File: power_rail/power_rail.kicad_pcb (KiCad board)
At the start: 2 copper layers, 100 x 50 mm, 18 parts, among them J1 Conn_01x06, J2 Conn_02x08_Row_Letter_Last, J3 Conn_02x08_Row_Letter_Last, J4 Conn_02x08_Row_Letter_Last, J5 Conn_02x08_Row_Letter_Last, J6 Conn_02x08_Row_Letter_Last, J7 Conn_02x08_Row_Letter_Last, J8 Conn_01x06

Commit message: VCA v. 2.0
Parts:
- added J11: Conn_01x01_Pin, power_rail_elements:Blade_3866B.68, F.Cu at (197.5, 96.4)
- added J12: Conn_01x01_Pin, power_rail_elements:Blade_3866B.68, F.Cu at (197.5, 102.1)
- added J13: Conn_01x01_Pin, power_rail_elements:Blade_3866B.68, F.Cu at (197.5, 107.9)
- added J14: Conn_01x01_Pin, power_rail_elements:Blade_3866B.68, F.Cu at (197.5, 113.6)
- added J15: Conn_01x01_Pin, power_rail_elements:Blade_3866B.68, F.Cu at (197.5, 119.3)
- added J16: Conn_01x01_Pin, power_rail_elements:Blade_3866B.68, F.Cu at (107.5, 96.4)
- added J17: Conn_01x01_Pin, power_rail_elements:Blade_3866B.68, F.Cu at (107.5, 102.1)
- added J18: Conn_01x01_Pin, power_rail_elements:Blade_3866B.68, F.Cu at (107.5, 107.9)
- added J19: Conn_01x01_Pin, power_rail_elements:Blade_3866B.68, F.Cu at (107.5, 113.6)
- added J20: Conn_01x01_Pin, power_rail_elements:Blade_3866B.68, F.Cu at (107.5, 119.3)
- added J9: Conn_02x08_Row_Letter_Last, Connector_IDC:IDC-Header_2x08_P2.54mm_Vertical, F.Cu at (167.8, 116.0)
- J1, J8: value Conn_01x06 -> Conn_01x01_Pin; footprint Connector_Wire:SolderWire-0.75sqmm_1x06_P4.8mm_D1.25mm_OD2.3mm -> power_rail_elements:Blade_3866B.68
- moved J8 94.3 mm to (107.5, 90.7), turned to 0 degrees
- moved J1 93.3 mm to (197.5, 90.7), turned to 0 degrees
- moved J5 7.28 mm to (156.2, 116.0)
- moved J4 5.32 mm to (144.6, 116.0)
- moved J6 4.29 mm to (179.4, 116.0)
- moved D2 3.83 mm to (176.9, 90.2)
- moved J3 3.77 mm to (133.0, 116.0)
- moved J2 3.31 mm to (121.4, 116.0)
- moved J7 3.31 mm to (190.9, 116.0)
- moved R1 3.24 mm to (121.3, 89.8)
- moved R2 2.65 mm to (165.1, 89.8)
- moved D1 2.48 mm to (133.1, 90.2)
- moved R3 2.02 mm to (143.1, 89.8)
- moved D3 1.37 mm to (155.0, 90.2)
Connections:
- J1 pad 1: /-12V -> /Gate
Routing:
- net /-12V: track 125.6 -> 219.0 mm
- net /+12V: track 119.3 -> 194.5 mm
- net /+5V: track 119.5 -> 179.9 mm
- net /Gate: track 100.8 -> 157.6 mm
- net /CV: track 98.9 -> 151.7 mm
- net Net-(D3-A): track 6.41 -> 5.18 mm
- net Net-(D2-K): track 5.60 -> 4.41 mm
- net Net-(D1-K): track 5.55 -> 4.36 mm

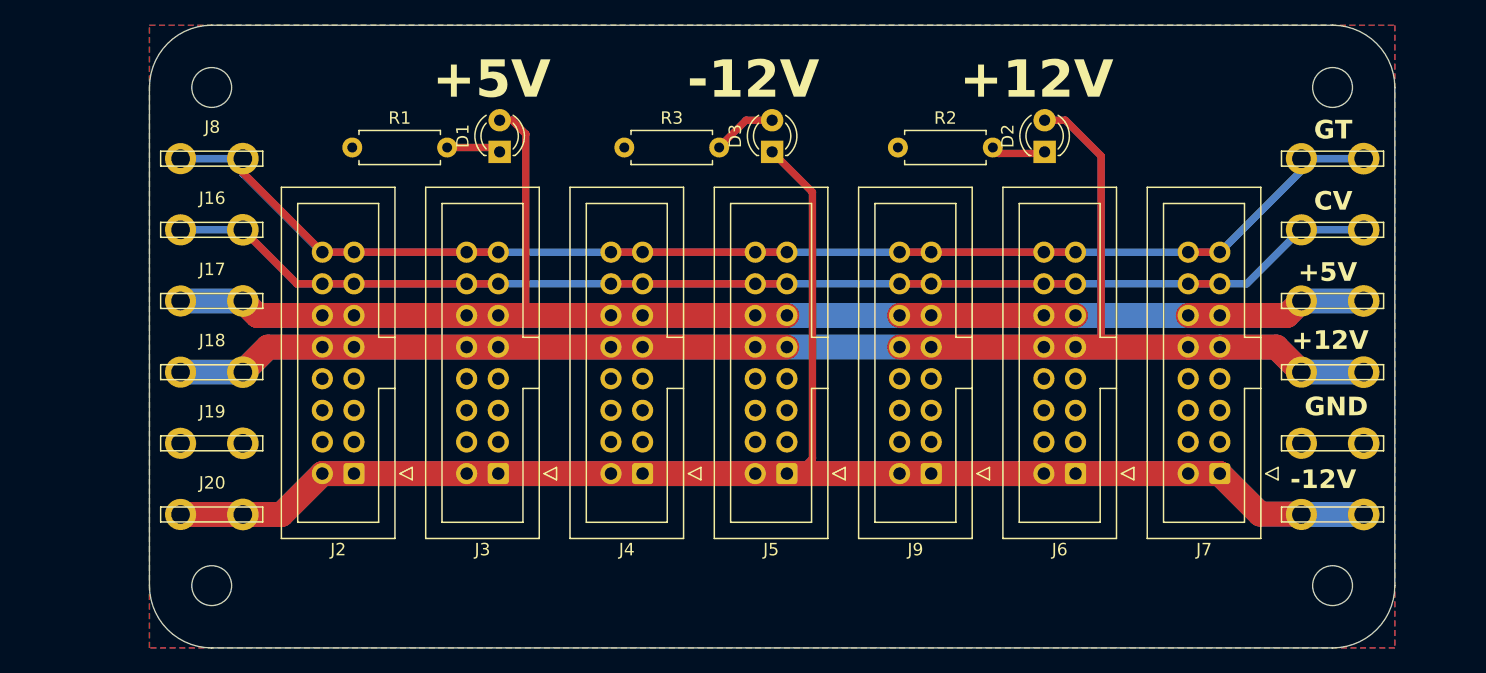
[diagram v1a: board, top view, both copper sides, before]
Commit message: Updated VCA-1 panel
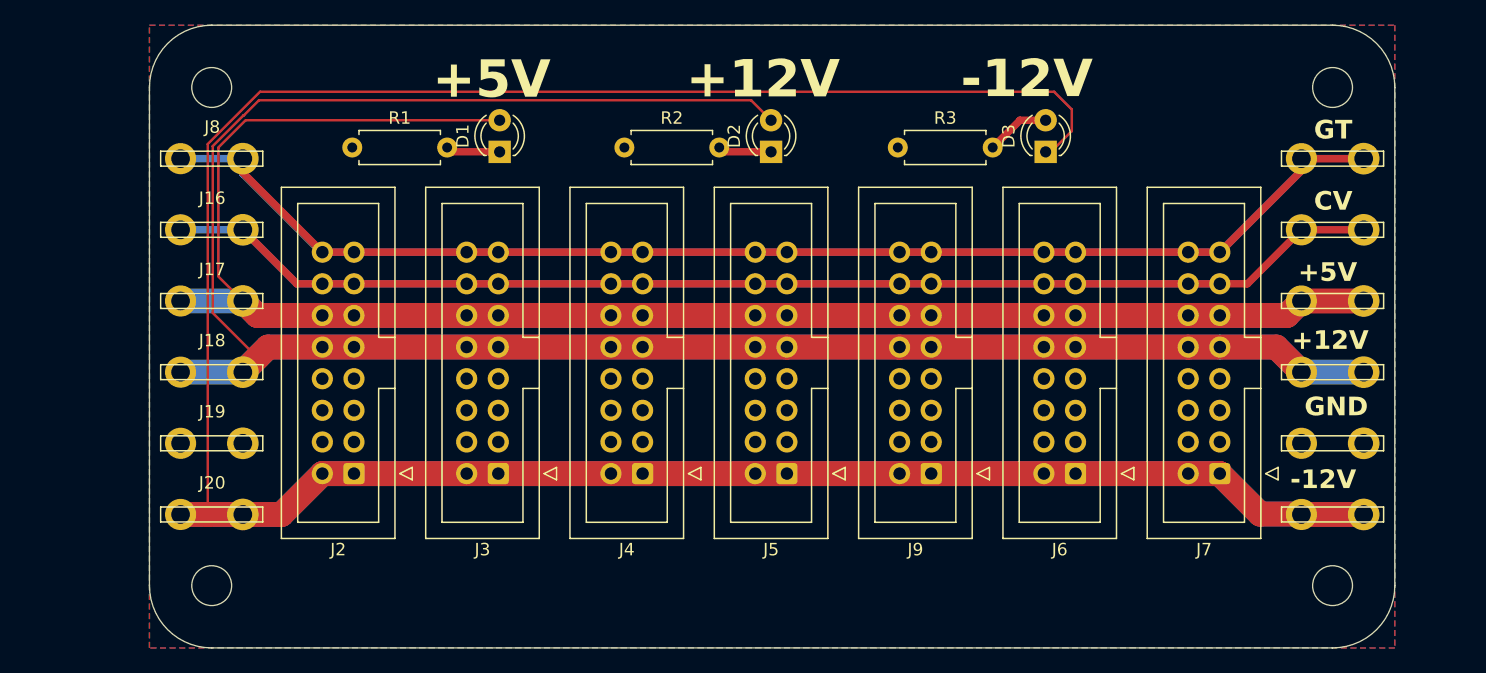
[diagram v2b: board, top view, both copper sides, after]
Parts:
- moved D2 22.0 mm to (154.9, 90.2)
- moved R2 22.0 mm to (143.1, 89.8)
- moved D3 22.0 mm to (177.0, 90.2)
- moved R3 22.0 mm to (165.1, 89.8)
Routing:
- net /-12V: track 219.0 -> 296.4 mm
- net /+12V: track 194.5 -> 248.8 mm
- net /+5V: track 179.9 -> 218.5 mm
- net /Gate: track 157.6 -> 194.9 mm
- net /CV: track 151.7 -> 178.8 mm

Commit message: Simulated exponential VCA control stage
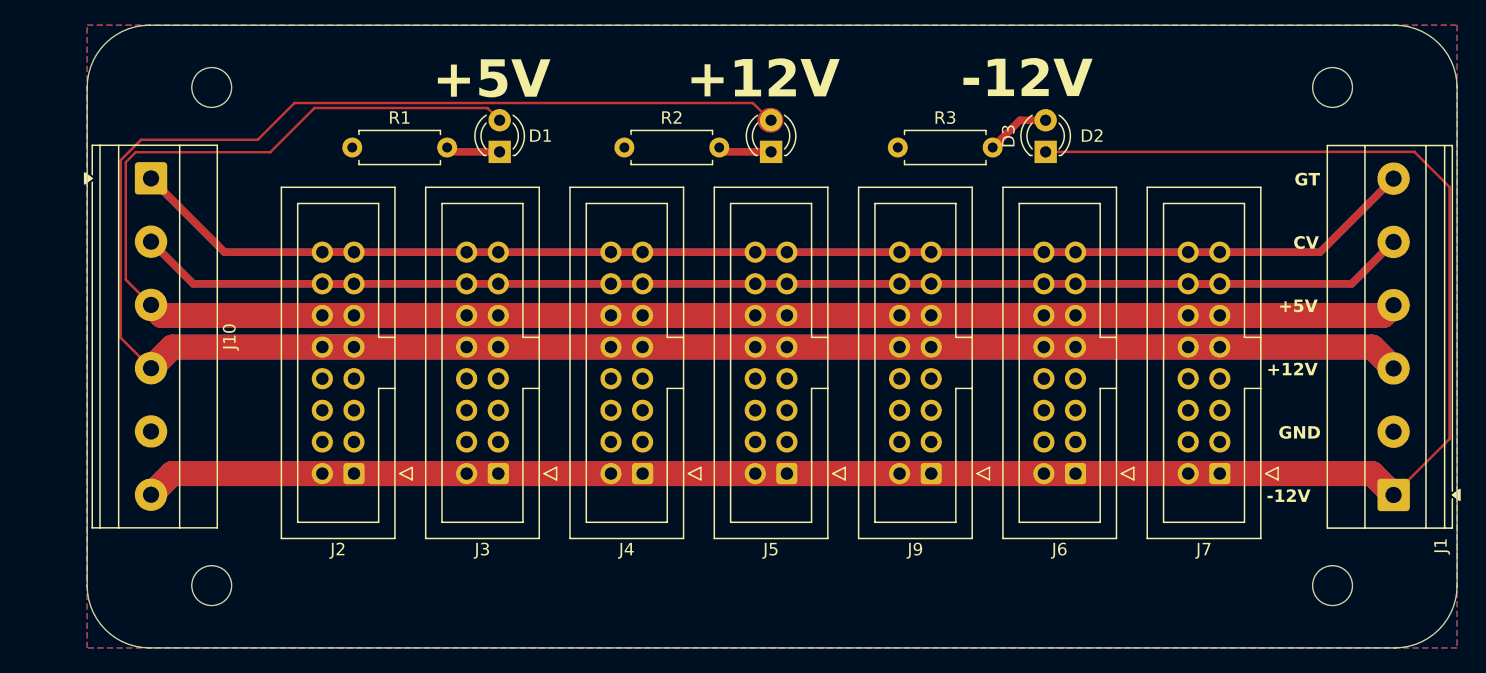
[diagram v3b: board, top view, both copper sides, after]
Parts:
- removed J11, J12, J13, J14, J15, J16, J17, J18, J19, J20, J8: Conn_01x01_Pin, power_rail_elements:Blade_3866B.68
- removed REF** (x4): MountingHole_3.2mm_M3, power_rail_elements:MountingHole_3.2mm_M3
- added H1: MountingHole, MountingHole:MountingHole_3.2mm_M3, F.Cu at (110.0, 85.0)
- added H2: MountingHole, MountingHole:MountingHole_3.2mm_M3, F.Cu at (200.0, 85.0)
- added H3: MountingHole, MountingHole:MountingHole_3.2mm_M3, F.Cu at (110.0, 125.0)
- added H4: MountingHole, MountingHole:MountingHole_3.2mm_M3, F.Cu at (200.0, 125.0)
- added J10: Conn_01x06_Socket, TerminalBlock_Phoenix:TerminalBlock_Phoenix_MKDS-1,5-6-5.08_1x06_P5.08mm_Horizontal, F.Cu at (105.1, 92.3)
- J1: value Conn_01x01_Pin -> Conn_01x06_Socket; footprint power_rail_elements:Blade_3866B.68 -> TerminalBlock_Phoenix:TerminalBlock_Phoenix_MKDS-1,5-6-5.08_1x06_P5.08mm_Horizontal
- moved J1 28.0 mm to (204.9, 117.7), turned to 90 degrees
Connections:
- J1 pad 1: /Gate -> /-12V
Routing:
- net /+5V: track 218.5 -> 250.5 mm
- net /CV: track 178.8 -> 210.2 mm
- net /+12V: track 248.8 -> 279.9 mm
- net /-12V: track 296.4 -> 267.6 mm
- net /Gate: track 194.9 -> 212.0 mm
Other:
- board size 100 x 50 mm -> 110 x 50 mm

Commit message: Exponential VCA ver. 1.2
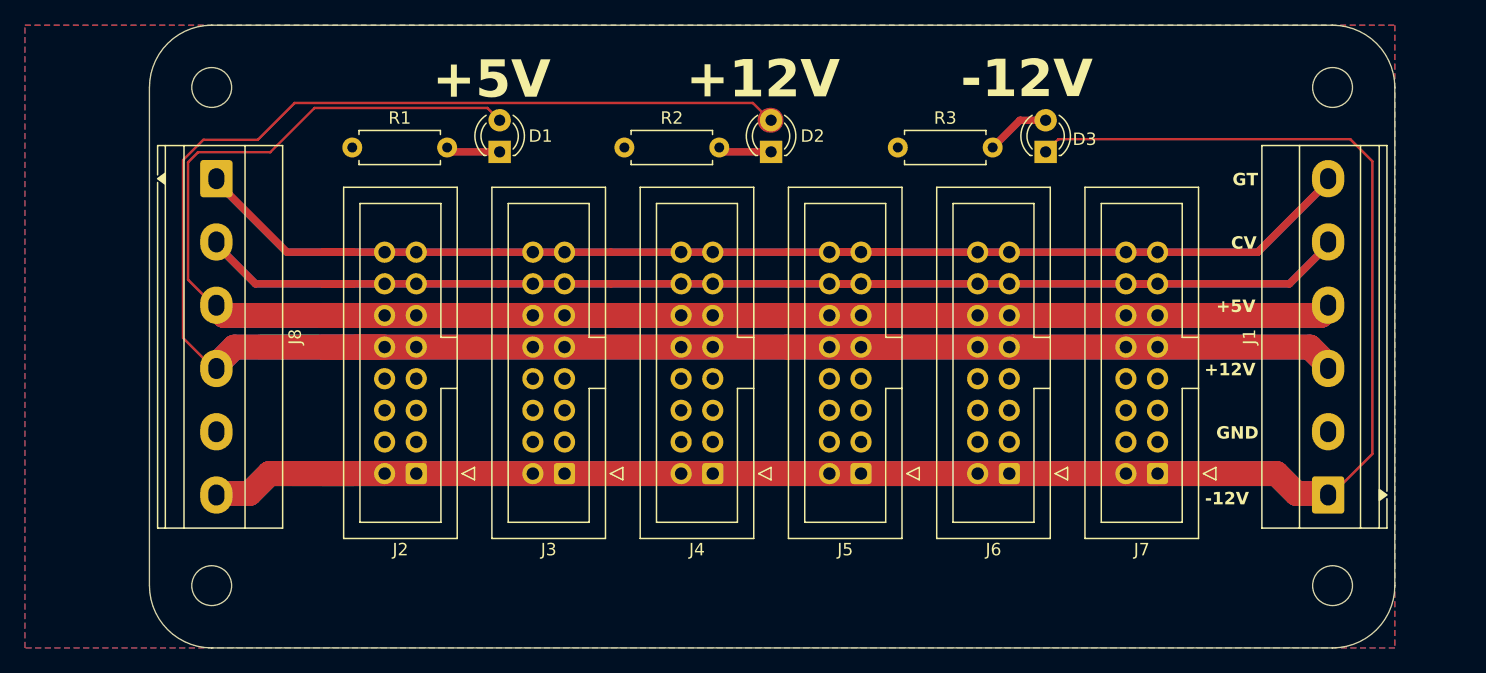
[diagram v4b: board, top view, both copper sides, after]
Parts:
- removed J10: Conn_01x06_Socket, TerminalBlock_Phoenix:TerminalBlock_Phoenix_MKDS-1,5-6-5.08_1x06_P5.08mm_Horizontal
- removed J9: Conn_02x08_Row_Letter_Last, Connector_IDC:IDC-Header_2x08_P2.54mm_Vertical
- added J8: Conn_01x06_Socket, power_rail_elements:TerminalBlock_Phoenix_MKDS-1,5-6-5.08_1x06_P5.08mm_Horizontal, F.Cu at (110.4, 92.3)
- J1: footprint TerminalBlock_Phoenix:TerminalBlock_Phoenix_MKDS-1,5-6-5.08_1x06_P5.08mm_Horizontal -> power_rail_elements:TerminalBlock_Phoenix_MKDS-1,5-6-5.08_1x06_P5.08mm_Horizontal
- moved J5 5.95 mm to (162.1, 116.0)
- moved J4 5.64 mm to (150.2, 116.0)
- moved J3 5.32 mm to (138.3, 116.0)
- moved J6 5.32 mm to (174.0, 116.0)
- moved J1 5.25 mm to (199.6, 117.7)
- moved J2 5.00 mm to (126.4, 116.0)
- moved J7 5.00 mm to (185.9, 116.0)
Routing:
- net /-12V: track 267.6 -> 257.2 mm
- net /+12V: track 279.9 -> 269.9 mm
- net /+5V: track 250.5 -> 240.5 mm
- net /Gate: track 212.0 -> 207.0 mm
- net /CV: track 210.2 -> 205.2 mm
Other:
- board size 110 x 50 mm -> 100 x 50 mm
